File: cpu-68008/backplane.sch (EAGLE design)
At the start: 24 parts, among them IC1 GAL22V10D, IC2 74HCT245, IC3 74HCT245, IC4 74HCT245, IC5 74HCT245

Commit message: routed level shifters to external connectors
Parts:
- added H1, H2, H3, H4: MOUNT-HOLE2.8, holes:MOUNT-HOLE2.8
- added SV101: (no value), con-lstb:MA10-2
- added SV102: (no value), con-lstb:MA20-2
- renumbered C1 to C202, C2 to C201, C203 to C101, C204 to C103, C205 to C104, C207 to C106, C208 to C107, C3 to C105, C4 to C102, IC1 to IC201, IC2 to IC101, IC3 to IC102, IC4 to IC103, IC5 to IC104, LED201 to LED102, LED202 to LED103, R114 to R103, R205 to R104, R206 to R105, SV201 to SV103, SV202 to SV104
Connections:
- removed net N$10: IC201.IN6
- removed net N$11: IC201.IN7
- net !AS: now also IC104A.A1, SV102.33; no longer IC104A.A6
- net !BERR: now also SV102.9
- net !BG: now also SV102.25
- net !BR: now also SV102.23
- net !BUF_DATA_OE: now also IC201.IO16; no longer IC201.IO15
- net !BUS_CS: now also SV101.7
- net !BUS_DTACK: now also SV101.6
- net !BUS_IRQ: now also SV101.5
- net !DS: now also IC104A.A2, SV102.31; no longer IC104A.A7
- net !DTACK: now also SV102.27
- net !HALT: now also SV102.17
- net !RESET: now also SV102.15
- net !SLOT_AS: now also IC104A.B1; no longer IC104A.B6
- net !SLOT_DS: now also IC104A.B2; no longer IC104A.B7
- net !VPA: now also SV102.11
- net +5V: now also SV101.1, SV101.2
- net A0: now also IC102A.A4, SV101.17; no longer IC102A.A1
- net A1: now also IC102A.A6, SV101.15; no longer IC102A.A2
- net A10: now also IC103A.A6, SV102.8; no longer IC103A.A3
- net A11: now also IC103A.A5, SV102.10; no longer IC103A.A4
- net A12: now also IC103A.A4, SV102.12; no longer IC103A.A5
- net A13: now also IC103A.A3, SV102.14; no longer IC103A.A6
- net A14: now also IC103A.A2, SV102.16; no longer IC103A.A7
- net A15: now also IC103A.A1, SV102.20; no longer IC103A.A8
- net A16: now also IC104A.A7, SV102.24; no longer IC104A.A1
- net A17: now also IC104A.A6, SV102.26; no longer IC104A.A2
- net A18: now also IC104A.A5, SV102.28; no longer IC104A.A3
- net A19: now also IC104A.A3, SV102.30; no longer IC104A.A4
- net A2: now also IC102A.A8, SV101.13; no longer IC102A.A3
- net A3: now also IC102A.A7, SV101.14; no longer IC102A.A4
- net A4: now also SV101.16
- net A5: now also IC102A.A3, SV101.18; no longer IC102A.A6
- net A6: now also IC102A.A2, SV101.20; no longer IC102A.A7
- net A7: now also IC102A.A1, SV102.2; no longer IC102A.A8
- net A8: now also IC103A.A8, SV102.4; no longer IC103A.A1
- net A9: now also IC103A.A7, SV102.6; no longer IC103A.A2
- net BUF_DATA_DIR: now also IC201.IO15; no longer IC201.IO16
- net CLK: now also SV102.21
- net D0: now also IC101A.A6, SV102.35; no longer IC101A.A1
- net D1: now also IC101A.A4, SV102.37; no longer IC101A.A2
- net D2: now also IC101A.A2, SV102.39; no longer IC101A.A3
- net D3: now also IC101A.A1, SV102.40; no longer IC101A.A4
- net D4: now also IC101A.A3, SV102.38; no longer IC101A.A5
- net D5: now also IC101A.A5, SV102.36; no longer IC101A.A6
- net D6: now also SV102.34
- net D7: now also SV102.32
- net E: now also SV102.13
- net FC0: now also SV101.19
- net FC1: now also SV102.1
- net FC2: now also SV102.3
- net GND: now also SV101.10, SV101.11, SV101.12, SV101.3, SV101.4, SV101.8, SV101.9, SV102.18, SV102.19, SV102.22, SV102.5, SV102.7
- net R/!W!: now also IC104A.A4, SV102.29; no longer IC104A.A5
- net SLOT_A0: now also IC102A.B4; no longer IC102A.B1
- net SLOT_A1: now also IC102A.B6; no longer IC102A.B2
- net SLOT_A10: now also IC103A.B6; no longer IC103A.B3
- net SLOT_A11: now also IC103A.B5; no longer IC103A.B4
- net SLOT_A12: now also IC103A.B4; no longer IC103A.B5
- net SLOT_A13: now also IC103A.B3; no longer IC103A.B6
- net SLOT_A14: now also IC103A.B2; no longer IC103A.B7
- net SLOT_A15: now also IC103A.B1; no longer IC103A.B8
- net SLOT_A16: now also IC104A.B7; no longer IC104A.B1
- net SLOT_A17: now also IC104A.B6; no longer IC104A.B2
- net SLOT_A18: now also IC104A.B5, IC201.IN5; no longer IC104A.B3
- net SLOT_A19: now also IC104A.B3, IC201.IN7; no longer IC104A.B4
- net SLOT_A2: now also IC102A.B8; no longer IC102A.B3
- net SLOT_A3: now also IC102A.B7; no longer IC102A.B4
- net SLOT_A5: now also IC102A.B3; no longer IC102A.B6
- net SLOT_A6: now also IC102A.B2; no longer IC102A.B7
- net SLOT_A7: now also IC102A.B1; no longer IC102A.B8
- net SLOT_A8: now also IC103A.B8; no longer IC103A.B1
- net SLOT_A9: now also IC103A.B7; no longer IC103A.B2
- net SLOT_D0: now also IC101A.B6; no longer IC101A.B1
- net SLOT_D1: now also IC101A.B4; no longer IC101A.B2
- net SLOT_D2: now also IC101A.B2; no longer IC101A.B3
- net SLOT_D3: now also IC101A.B1; no longer IC101A.B4
- net SLOT_D4: now also IC101A.B3; no longer IC101A.B5
- net SLOT_D5: now also IC101A.B5; no longer IC101A.B6
- net SLOT_R/!W!: now also IC104A.B4, IC201.IN6; no longer IC104A.B5, IC201.IN5
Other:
- note added: "1x 100nF for each IC101-4 1x 10µF shared between IC101-4"
- note added: "SV103/104 are duplicated as SV101/102 for a logic analyzer to be attached"
- note removed: "1x 100nF for each IC, osc, and connector"

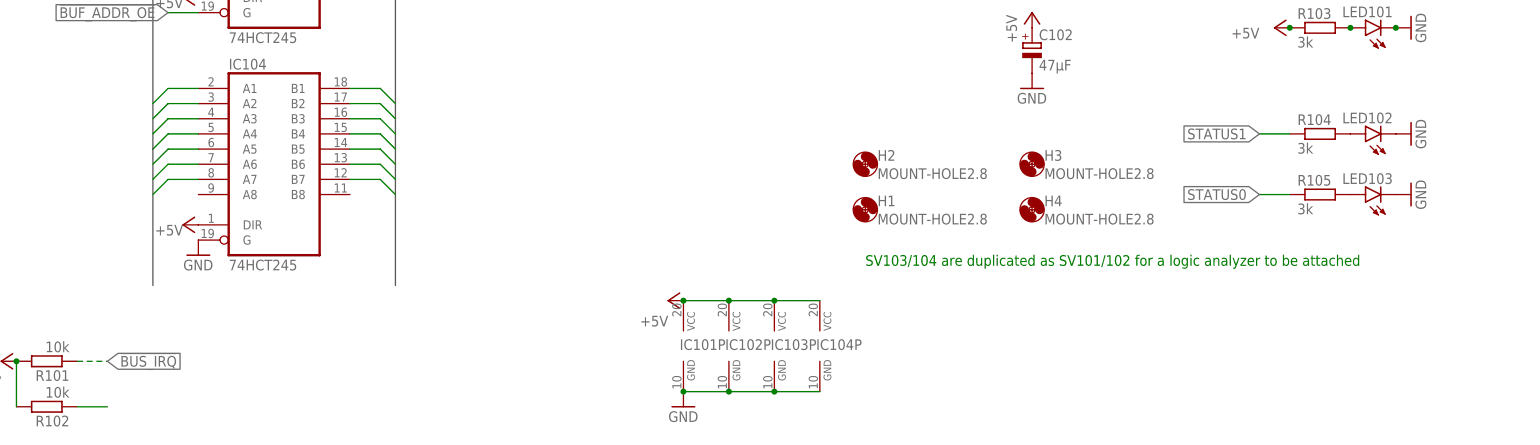
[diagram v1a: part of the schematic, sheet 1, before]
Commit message: finished routing backplane
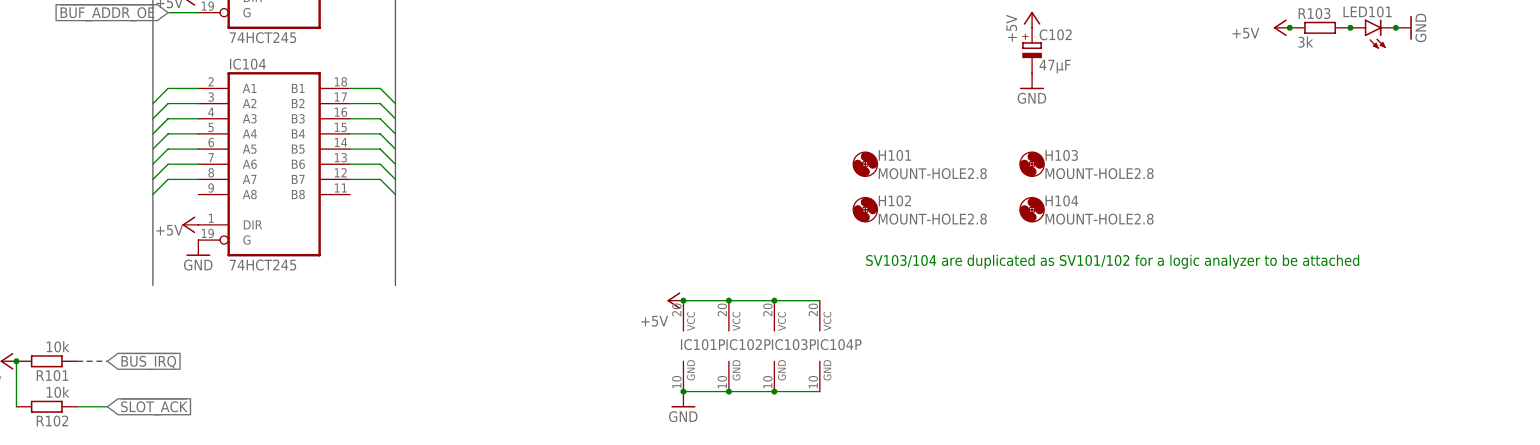
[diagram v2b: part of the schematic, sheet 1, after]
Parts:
- removed LED102, LED103: (no value), led:LEDCHIPLED_1206
- removed R104, R105: 3k, rcl:R-EU_R2012
- added C301, C302, C303, C304: 100nF, rcl:C-EUC0805
- added C305, C306: 10µF, rcl:CPOL-EUSMCB
- added LED301, LED302, LED303, LED304: (no value), led:LEDCHIPLED_1206
- added R301, R302, R303, R304: 3k, rcl:R-EU_R2012
- added SV301, SV302, SV303, SV304: (no value), con-lsta:FE20-2
- added WEED301: WEED, 68komputer:WEED
- renumbered H1 to H102, H2 to H101, H3 to H103, H4 to H104
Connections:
- removed net !HALT1: R102.1
- removed net N$16: IC201.IN13
- removed net N$7: LED102.A, R104.2
- removed net N$9: LED103.A, R105.2
- removed net STATUS0: R105.1
- removed net STATUS1: R104.1
- new net !SLOT_ACK: IC201.IN13, R102.1, SV301.24, SV302.24, SV303.24, SV304.24
- new net N$1: LED302.A, R302.2
- new net N$2: LED301.A, R301.2
- new net N$3: LED304.A, R304.2
- new net N$5: LED303.A, R303.2
- net !BUS_IRQ: now also SV301.6, SV302.6, SV303.6, SV304.6
- net !SLOT_AS: now also SV301.32, SV302.32, SV303.32, SV304.32
- net !SLOT_CS0: now also IC201.IO23, LED301.C, SV301.5; no longer IC201.IO20
- net !SLOT_CS1: now also IC201.IO22, LED302.C, SV303.5; no longer IC201.IO21
- net !SLOT_CS2: now also IC201.IO21, LED303.C, SV302.5; no longer IC201.IO22
- net !SLOT_CS3: now also IC201.IO20, LED304.C, SV304.5; no longer IC201.IO23
- net !SLOT_DS: now also SV301.31, SV302.31, SV303.31, SV304.31
- net +5V: now also C301.1, C302.1, C303.1, C304.1, C305.+, C306.+, R301.1, R302.1, R303.1, R304.1, SV301.1, SV301.2, SV302.1, SV302.2, SV303.1, SV303.2, SV304.1, SV304.2
- net GND: now also C301.2, C302.2, C303.2, C304.2, C305.-, C306.-, SV301.25, SV301.26, SV301.27, SV301.28, SV301.3, SV301.4, SV302.25, SV302.26, SV302.27, SV302.28, SV302.3, SV302.4, SV303.25, SV303.26, SV303.27, SV303.28, SV303.3, SV303.4, SV304.25, SV304.26, SV304.27, SV304.28, SV304.3, SV304.4; no longer LED102.C, LED103.C
- net SLOT_A0: now also SV301.12, SV302.12, SV303.12, SV304.12
- net SLOT_A1: now also SV301.10, SV302.10, SV303.10, SV304.10
- net SLOT_A10: now also SV301.18, SV302.18, SV303.18, SV304.18
- net SLOT_A11: now also SV301.17, SV302.17, SV303.17, SV304.17
- net SLOT_A12: now also SV301.20, SV302.20, SV303.20, SV304.20
- net SLOT_A13: now also SV301.19, SV302.19, SV303.19, SV304.19
- net SLOT_A14: now also SV301.22, SV302.22, SV303.22, SV304.22
- net SLOT_A15: now also SV301.21, SV302.21, SV303.21, SV304.21
- net SLOT_A2: now also SV301.8, SV302.8, SV303.8, SV304.8
- net SLOT_A3: now also SV301.7, SV302.7, SV303.7, SV304.7
- net SLOT_A4: now also SV301.9, SV302.9, SV303.9, SV304.9
- net SLOT_A5: now also SV301.11, SV302.11, SV303.11, SV304.11
- net SLOT_A6: now also SV301.14, SV302.14, SV303.14, SV304.14
- net SLOT_A7: now also SV301.13, SV302.13, SV303.13, SV304.13
- net SLOT_A8: now also SV301.16, SV302.16, SV303.16, SV304.16
- net SLOT_A9: now also SV301.15, SV302.15, SV303.15, SV304.15
- net SLOT_D0: now also SV301.35, SV302.35, SV303.35, SV304.35
- net SLOT_D1: now also SV301.37, SV302.37, SV303.37, SV304.37
- net SLOT_D2: now also SV301.39, SV302.39, SV303.39, SV304.39
- net SLOT_D3: now also SV301.40, SV302.40, SV303.40, SV304.40
- net SLOT_D4: now also SV301.38, SV302.38, SV303.38, SV304.38
- net SLOT_D5: now also SV301.36, SV302.36, SV303.36, SV304.36
- net SLOT_D6: now also SV301.34, SV302.34, SV303.34, SV304.34
- net SLOT_D7: now also SV301.33, SV302.33, SV303.33, SV304.33
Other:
- note added: "One 10µF per two slots"
- note added: "Slot 1"
- note added: "Slot 2"
- note added: "Slot 3"
- note added: "Slot 4"

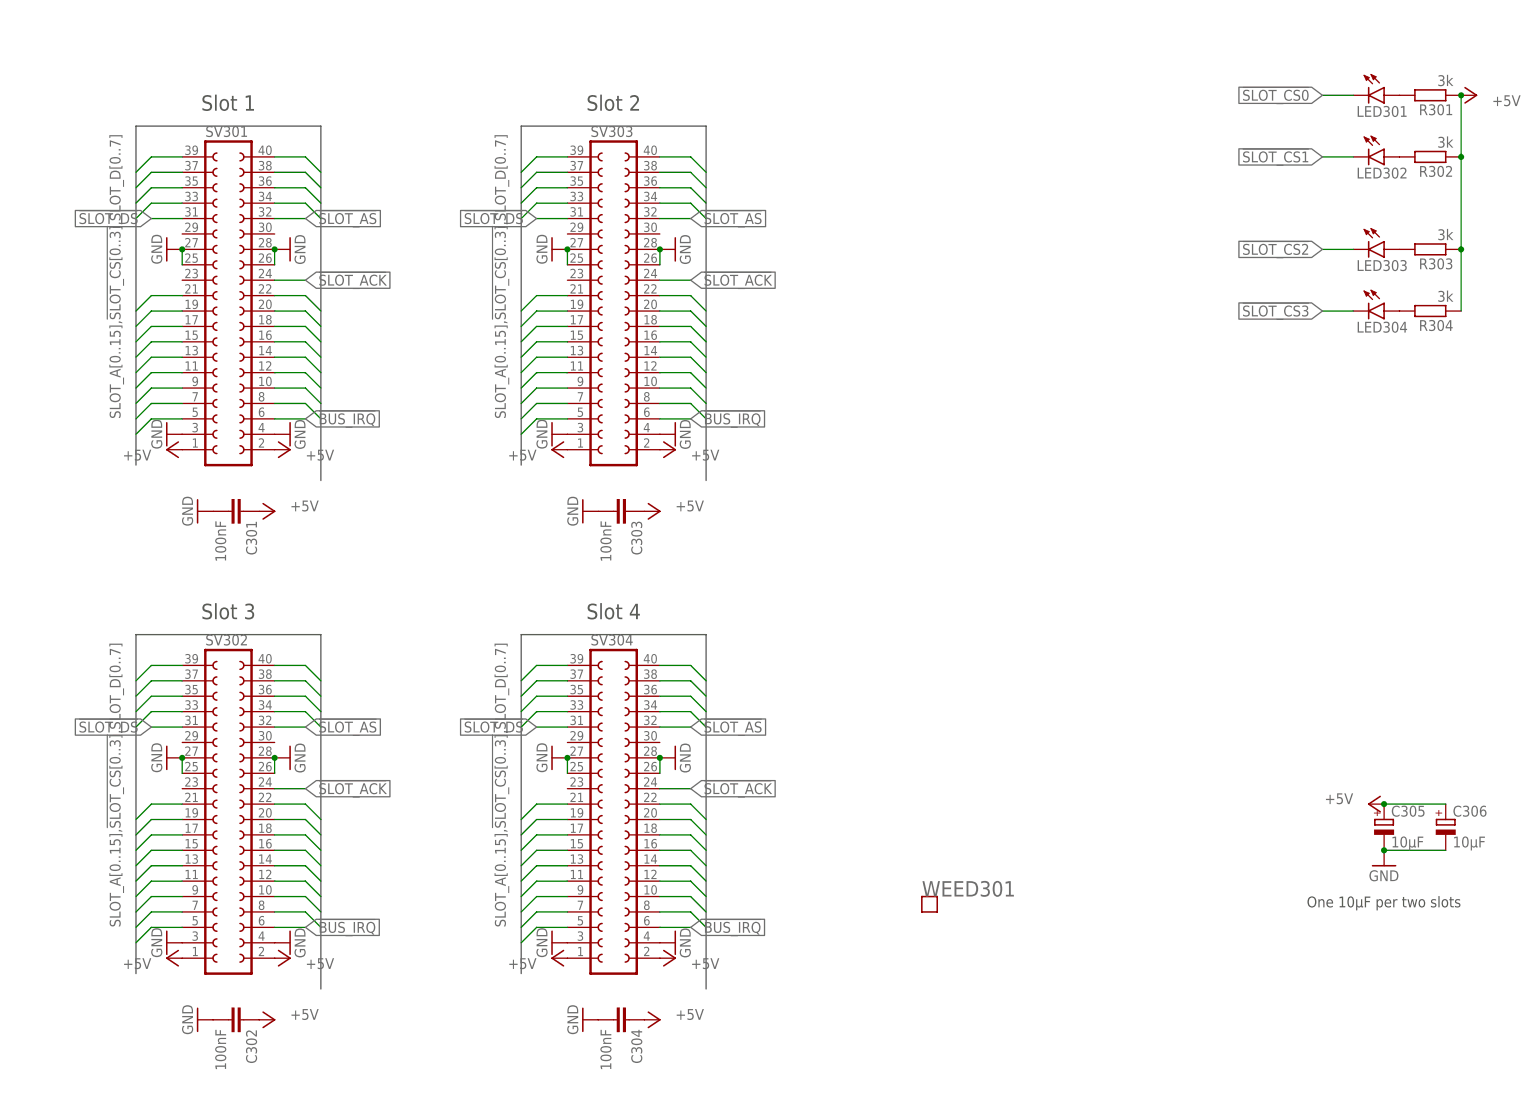
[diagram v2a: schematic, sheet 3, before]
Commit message: added r/w and reset to backplane; fixed some missing mouser p/n on cpu board
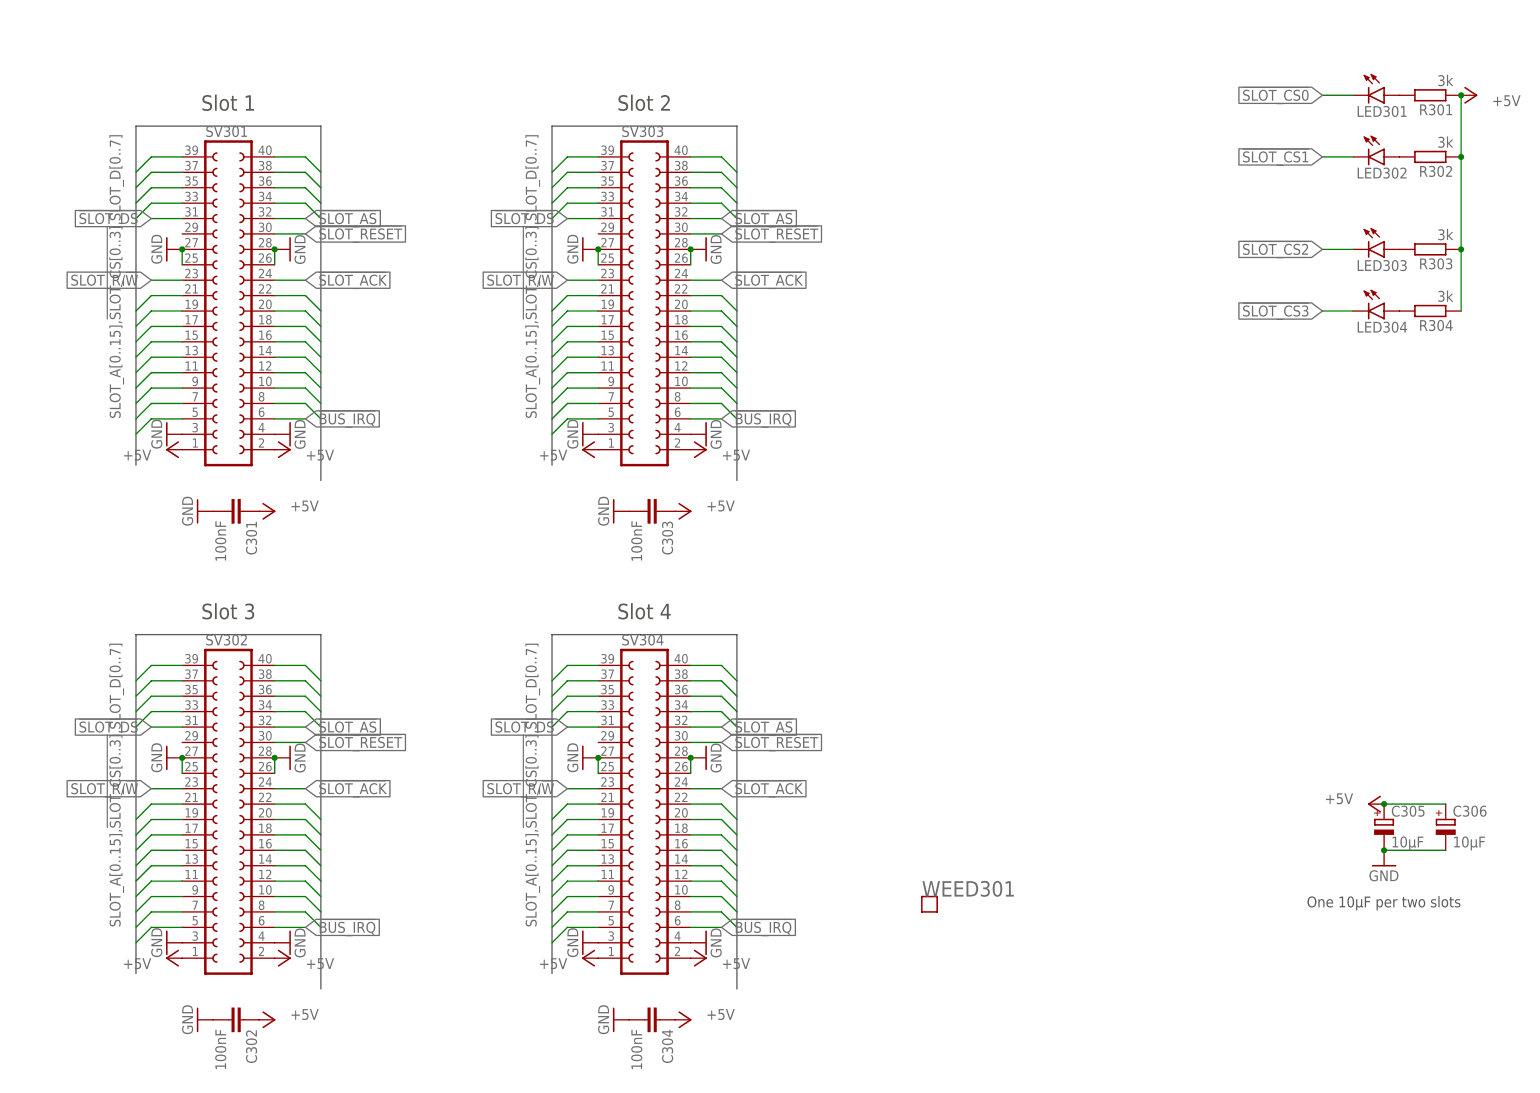
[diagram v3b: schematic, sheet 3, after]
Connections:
- removed net N$12: IC201.IN8
- new net !SLOT_RESET: IC104A.B8, IC201.IN8, SV301.30, SV302.30, SV303.30, SV304.30
- net !RESET: now also IC104A.A8
- net SLOT_R/!W!: now also SV301.23, SV302.23, SV303.23, SV304.23
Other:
- moved on the sheet: C303, C304, SV303, SV304
